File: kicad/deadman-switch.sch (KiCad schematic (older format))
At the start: 7 parts, among them SW1 SW_Push

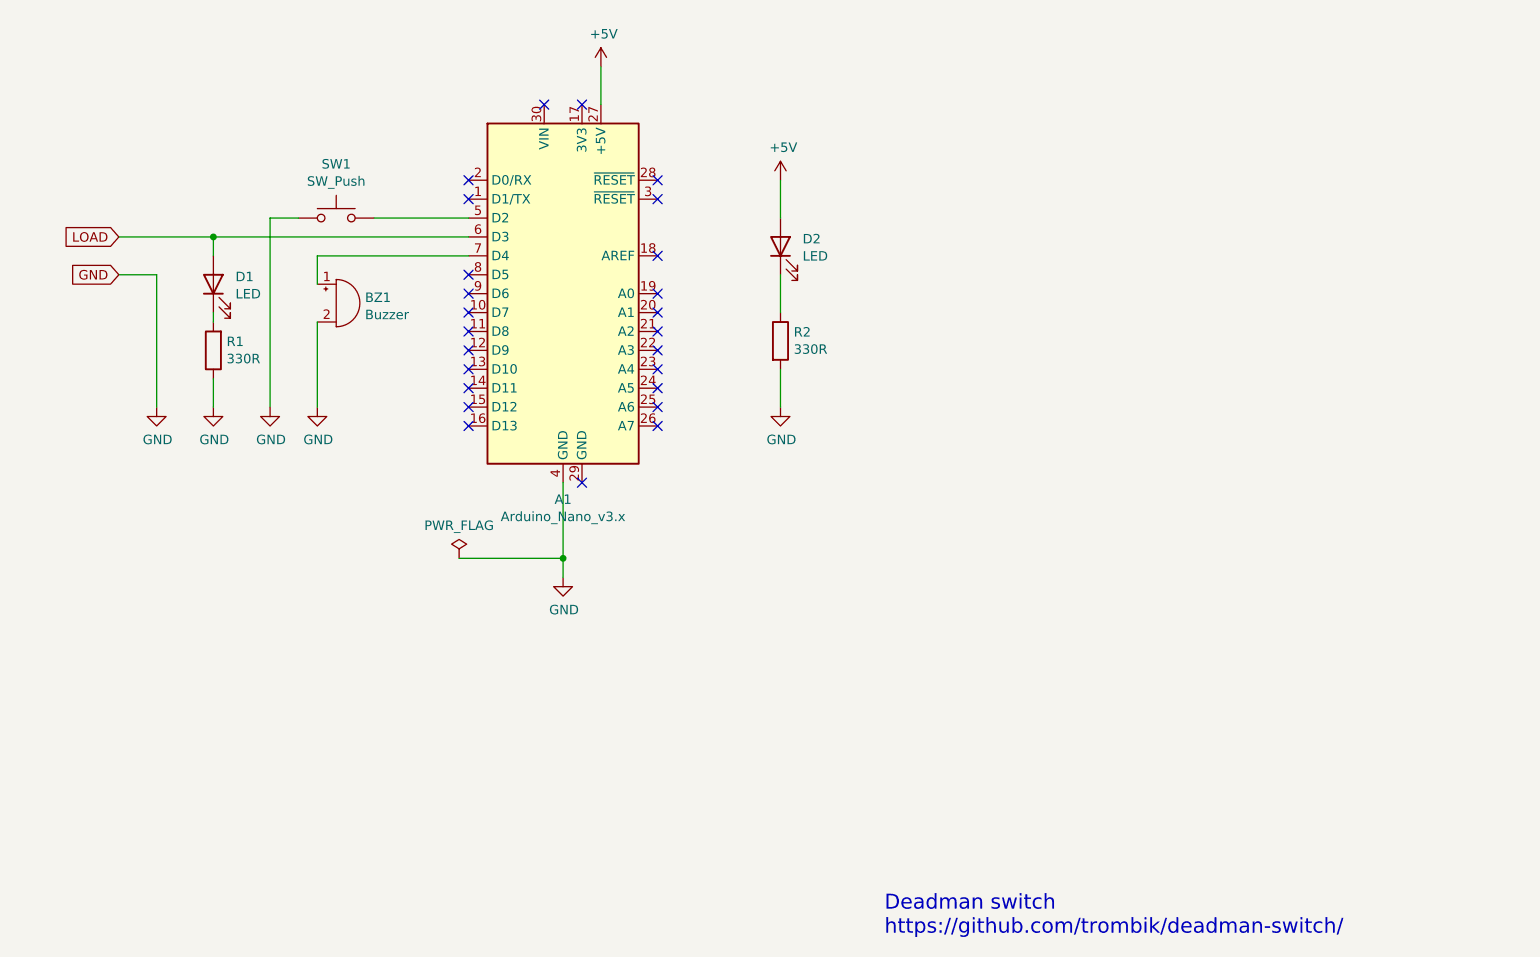
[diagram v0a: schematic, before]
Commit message: update schematic
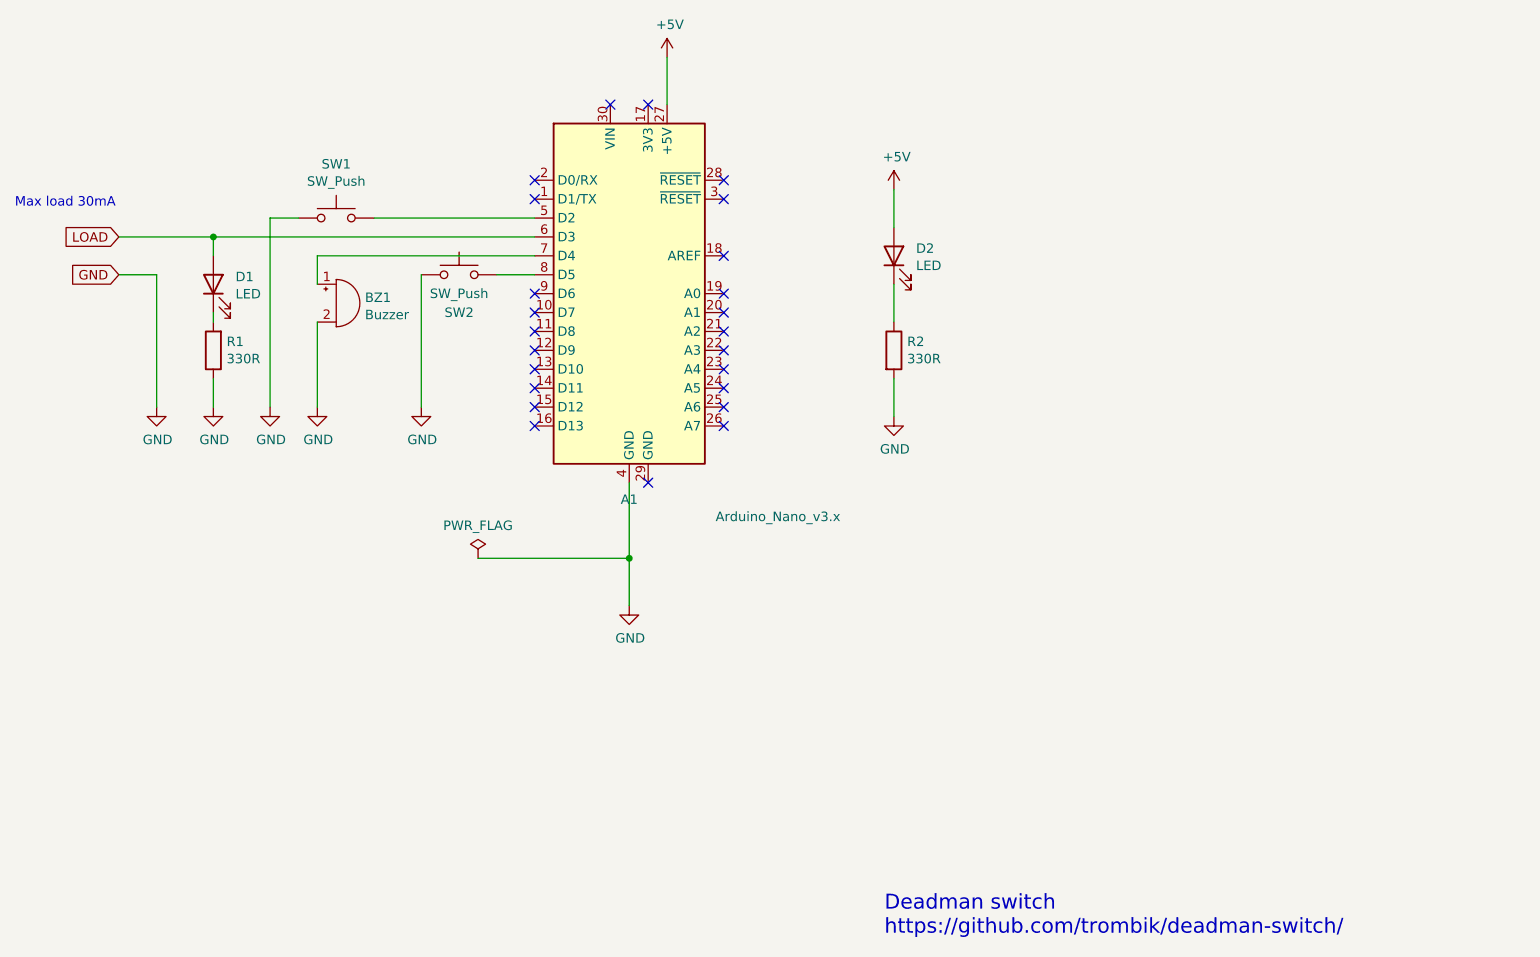
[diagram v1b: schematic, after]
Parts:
- added SW2: SW_Push, symbol Switch:SW_Push
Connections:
- net GND: now also SW2.1
- net at A1.8 (D5): now also SW2.2
- no-connect marks 25 -> 24
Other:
- note added: "Max load 30mA"
- moved on the sheet: A1, D2, R2
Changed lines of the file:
@@
 $EndDescr
-$Comp
-L MCU_Module:Arduino_Nano_v3.x A1
-U 1 1 5F365897
-P 6050 3550
-F 0 "A1" H 6050 2461 50  0000 C CNN
-F 1 "Arduino_Nano_v3.x" H 6050 2370 50  0000 C CNN
-F 2 "Module:Arduino_Nano" H 6050 3550 50  0001 C CIN
-F 3 "http://www.mouser.com/pdfdocs/Gravitech_Arduino_Nano3_0.pdf" H 6050 3550 50  0001 C CNN
-	1    6050 3550
-	1    0    0    -1
-$EndComp
 $Comp
 L Switch:SW_Push SW1
@@
 Wire Wire Line
 	4500 3150 4650 3150
-Wire Wire Line
-	5050 3150 5550 3150
 $Comp
 L Device:LED D1
@@
 $EndComp
 Wire Wire Line
-	4200 3250 5550 3250
-Wire Wire Line
-	5550 3350 4750 3350
-Wire Wire Line
 	4750 3350 4750 3500
 Wire Wire Line
 	4750 3700 4750 4150
-$Comp
-L power:+5V #PWR05
-U 1 1 5F399D20
-P 6250 2350
-F 0 "#PWR05" H 6250 2200 50  0001 C CNN
-F 1 "+5V" H 6265 2523 50  0000 C CNN
-F 2 "" H 6250 2350 50  0001 C CNN
-F 3 "" H 6250 2350 50  0001 C CNN
-	1    6250 2350
-	1    0    0    -1
-$EndComp
-$Comp
-L power:GND #PWR04
-U 1 1 5F39B7D9
-P 6050 5050
-F 0 "#PWR04" H 6050 4800 50  0001 C CNN
-F 1 "GND" H 6055 4877 50  0000 C CNN
-F 2 "" H 6050 5050 50  0001 C CNN
-F 3 "" H 6050 5050 50  0001 C CNN
-	1    6050 5050
-	1    0    0    -1
-$EndComp
-Wire Wire Line
-	6050 4550 6050 4950
-Wire Wire Line
-	6250 2350 6250 2550
 $Comp
 L Device:LED D2
 U 1 1 5F39F628
-P 7200 3300
-F 0 "D2" V 7239 3183 50  0000 R CNN
-F 1 "LED" V 7148 3183 50  0000 R CNN
-F 2 "" H 7200 3300 50  0001 C CNN
-F 3 "~" H 7200 3300 50  0001 C CNN
-	1    7200 3300
+P 7800 3350
+F 0 "D2" V 7839 3233 50  0000 R CNN
+F 1 "LED" V 7748 3233 50  0000 R CNN
+F 2 "" H 7800 3350 50  0001 C CNN
+F 3 "~" H 7800 3350 50  0001 C CNN
+	1    7800 3350
 	0    -1   -1   0
 $EndComp
@@
 L power:+5V #PWR06
 U 1 1 5F3A0C21
-P 7200 2950
-F 0 "#PWR06" H 7200 2800 50  0001 C CNN
-F 1 "+5V" H 7215 3123 50  0000 C CNN
-F 2 "" H 7200 2950 50  0001 C CNN
-F 3 "" H 7200 2950 50  0001 C CNN
-	1    7200 2950
+P 7800 3000
+F 0 "#PWR06" H 7800 2850 50  0001 C CNN
+F 1 "+5V" H 7815 3173 50  0000 C CNN
+F 2 "" H 7800 3000 50  0001 C CNN
+F 3 "" H 7800 3000 50  0001 C CNN
+	1    7800 3000
 	1    0    0    -1
 $EndComp
@@
 L power:GND #PWR07
 U 1 1 5F3A1198
-P 7200 4150
-F 0 "#PWR07" H 7200 3900 50  0001 C CNN
-F 1 "GND" H 7205 3977 50  0000 C CNN
-F 2 "" H 7200 4150 50  0001 C CNN
-F 3 "" H 7200 4150 50  0001 C CNN
-	1    7200 4150
+P 7800 4200
+F 0 "#PWR07" H 7800 3950 50  0001 C CNN
+F 1 "GND" H 7805 4027 50  0000 C CNN
+F 2 "" H 7800 4200 50  0001 C CNN
+F 3 "" H 7800 4200 50  0001 C CNN
+	1    7800 4200
 	1    0    0    -1
 $EndComp
@@
 L Device:R R2
 U 1 1 5F3A2DBF
-P 7200 3800
-F 0 "R2" H 7270 3846 50  0000 L CNN
-F 1 "330R" H 7270 3755 50  0000 L CNN
-F 2 "" V 7130 3800 50  0001 C CNN
-F 3 "~" H 7200 3800 50  0001 C CNN
-	1    7200 3800
-	1    0    0    -1
-$EndComp
-Wire Wire Line
-	7200 2950 7200 3150
-Wire Wire Line
-	7200 3450 7200 3650
-Wire Wire Line
-	7200 3950 7200 4150
+P 7800 3850
+F 0 "R2" H 7870 3896 50  0000 L CNN
+F 1 "330R" H 7870 3805 50  0000 L CNN
+F 2 "" V 7730 3850 50  0001 C CNN
+F 3 "~" H 7800 3850 50  0001 C CNN
+	1    7800 3850
+	1    0    0    -1
+$EndComp
+Wire Wire Line
+	7800 3000 7800 3200
+Wire Wire Line
+	7800 3500 7800 3700
+Wire Wire Line
+	7800 4000 7800 4200
 Wire Wire Line
 	4200 4150 4200 4000
@@
 Wire Wire Line
 	3700 3250 4200 3250
-Connection ~ 4200 3250
 Wire Wire Line
 	4200 3700 4200 3650
@@
 	1    0    0    -1
 $EndComp
-NoConn ~ 5550 2950
-NoConn ~ 5550 3050
-NoConn ~ 5550 3450
-NoConn ~ 5550 3550
-NoConn ~ 5550 3650
-NoConn ~ 5550 3750
-NoConn ~ 5550 3850
-NoConn ~ 5550 3950
-NoConn ~ 5550 4050
-NoConn ~ 5550 4150
-NoConn ~ 5550 4250
-NoConn ~ 6550 4250
-NoConn ~ 6550 4150
-NoConn ~ 6550 4050
-NoConn ~ 6550 3950
-NoConn ~ 6550 3850
-NoConn ~ 6550 3750
-NoConn ~ 6550 3550
-NoConn ~ 6550 3650
-NoConn ~ 6550 2950
-NoConn ~ 6550 3050
-NoConn ~ 6150 2550
-NoConn ~ 5950 2550
-NoConn ~ 6150 4550
-NoConn ~ 6550 3350
+Text Notes 7750 6950 0    79   ~ 0
+Deadman switch\nhttps://github.com/trombik/deadman-switch/
+Connection ~ 4200 3250
+Wire Wire Line
+	5050 3150 5900 3150
+Wire Wire Line
+	4200 3250 5900 3250
+Wire Wire Line
+	5900 3350 4750 3350
+$Comp
+L power:+5V #PWR05
+U 1 1 5F399D20
+P 6600 2300
+F 0 "#PWR05" H 6600 2150 50  0001 C CNN
+F 1 "+5V" H 6615 2473 50  0000 C CNN
+F 2 "" H 6600 2300 50  0001 C CNN
+F 3 "" H 6600 2300 50  0001 C CNN
+	1    6600 2300
+	1    0    0    -1
+$EndComp
+$Comp
+L power:GND #PWR04
+U 1 1 5F39B7D9
+P 6400 5200
+F 0 "#PWR04" H 6400 4950 50  0001 C CNN
+F 1 "GND" H 6405 5027 50  0000 C CNN
+F 2 "" H 6400 5200 50  0001 C CNN
+F 3 "" H 6400 5200 50  0001 C CNN
+	1    6400 5200
+	1    0    0    -1
+$EndComp
+Wire Wire Line
+	6400 4550 6400 4950
+Wire Wire Line
+	6600 2300 6600 2550
+NoConn ~ 5900 2950
+NoConn ~ 5900 3050
+NoConn ~ 5900 3550
+NoConn ~ 5900 3650
+NoConn ~ 5900 3750
+NoConn ~ 5900 3850
+NoConn ~ 5900 3950
+NoConn ~ 5900 4050
+NoConn ~ 5900 4150
+NoConn ~ 5900 4250
+NoConn ~ 6900 4250
+NoConn ~ 6900 4150
+NoConn ~ 6900 4050
+NoConn ~ 6900 3950
+NoConn ~ 6900 3850
+NoConn ~ 6900 3750
+NoConn ~ 6900 3550
+NoConn ~ 6900 3650
+NoConn ~ 6900 2950
+NoConn ~ 6900 3050
+NoConn ~ 6500 2550
+NoConn ~ 6300 2550
+NoConn ~ 6500 4550
+NoConn ~ 6900 3350
 $Comp
 L power:PWR_FLAG #FLG0101
 U 1 1 5F3CACE7
-P 5500 4950
-F 0 "#FLG0101" H 5500 5025 50  0001 C CNN
-F 1 "PWR_FLAG" H 5500 5123 50  0000 C CNN
-F 2 "" H 5500 4950 50  0001 C CNN
-F 3 "~" H 5500 4950 50  0001 C CNN
-	1    5500 4950
-	1    0    0    -1
-$EndComp
-Wire Wire Line
-	5500 4950 6050 4950
-Connection ~ 6050 4950
-Wire Wire Line
-	6050 4950 6050 5050
-Text Notes 7750 6950 0    79   ~ 0
-Deadman switch\nhttps://github.com/trombik/deadman-switch/
+P 5600 4950
+F 0 "#FLG0101" H 5600 5025 50  0001 C CNN
+F 1 "PWR_FLAG" H 5600 5123 50  0000 C CNN
+F 2 "" H 5600 4950 50  0001 C CNN
+F 3 "~" H 5600 4950 50  0001 C CNN
+	1    5600 4950
+	1    0    0    -1
+$EndComp
+Wire Wire Line
+	5600 4950 6400 4950
+Connection ~ 6400 4950
+Wire Wire Line
+	6400 4950 6400 5200
+$Comp
+L MCU_Module:Arduino_Nano_v3.x A1
+U 1 1 5F365897
+P 6400 3550
+F 0 "A1" H 6400 2461 50  0000 C CNN
+F 1 "Arduino_Nano_v3.x" H 7187 2370 50  0000 C CNN
+F 2 "Module:Arduino_Nano" H 6400 3550 50  0001 C CIN
+F 3 "http://www.mouser.com/pdfdocs/Gravitech_Arduino_Nano3_0.pdf" H 6400 3550 50  0001 C CNN
+	1    6400 3550
+	1    0    0    -1
+$EndComp
+Text Notes 3150 3100 0    50   ~ 0
+Max load 30mA
+$Comp
+L power:GND #PWR08
+U 1 1 5F594654
+P 5300 4150
+F 0 "#PWR08" H 5300 3900 50  0001 C CNN
+F 1 "GND" H 5305 3977 50  0000 C CNN
+F 2 "" H 5300 4150 50  0001 C CNN
+F 3 "" H 5300 4150 50  0001 C CNN
+	1    5300 4150
+	1    0    0    -1
+$EndComp
+Wire Wire Line
+	5300 3450 5300 4150
+Wire Wire Line
+	5700 3450 5900 3450
+$Comp
+L Switch:SW_Push SW2
+U 1 1 5F592715
+P 5500 3450
+F 0 "SW2" H 5500 3250 50  0000 C CNN
+F 1 "SW_Push" H 5500 3350 50  0000 C CNN
+F 2 "" H 5500 3650 50  0001 C CNN
+F 3 "~" H 5500 3650 50  0001 C CNN
+	1    5500 3450
+	1    0    0    -1
+$EndComp
 $EndSCHEMATC
